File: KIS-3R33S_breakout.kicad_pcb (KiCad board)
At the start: 2 copper layers, 5 parts, among them P1 Screw terminal, P2 Screw terminal, U1 KIS-3R33S_modif

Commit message: Throwing parts around.
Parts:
- added C1: 1mF, 25V, Capacitors_SMD:c_elec_SMD_12.5x13.5, F.Cu at (172.0, 100.0)
- moved P2 16.6 mm to (184.7, 100.0)
- moved R1 13.0 mm to (182.3, 91.9)
- moved P1 10.8 mm to (130.6, 100.0)
- moved U1 9.20 mm to (150.0, 100.0)
- moved D1 7.07 mm to (186.8, 91.9)
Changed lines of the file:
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@@
 (kicad_pcb (version 4) (host pcbnew "(2015-05-01 BZR 5636)-product")
   (general
-    (links 8)
-    (no_connects 8)
-    (area 116.607142 92.155 182.14846 121.75)
+    (links 10)
+    (no_connects 10)
+    (area 124.607142 87.3 190.642858 112.6)
     (thickness 1.6)
     (drawings 0)
     (tracks 0)
     (zones 0)
-    (modules 5)
+    (modules 6)
     (nets 5)
   )
@@
   )
   (module DC-DC-modules:KIS-3R33S (layer F.Cu)
-    (at 149 109.15)
+    (at 150 100)
     (descr ./Docs/KIS-3R33S.pdf)
     (tags "DC-DC, buck, KIS-3R33S")
-    (fp_text reference U1 (at 0.05 11.6) (layer F.SilkS)
+    (fp_text reference U1 (at 0.05 11.6) (layer F.SilkS) hide
       (effects (font (size 1 1) (thickness 0.2)))
     )
@@
   )
   (module LEDs:LED-0805 (layer F.Cu)
-    (at 180.3 94.55)
+    (at 186.85 91.9)
     (descr "LED 0805 smd package")
     (tags "LED 0805 SMD")
     (attr smd)
-    (fp_text reference D1 (at 0 -1.27) (layer F.SilkS)
+    (fp_text reference D1 (at -0.1 1.8) (layer F.SilkS)
       (effects (font (size 1 1) (thickness 0.15)))
     )
@@
   )
   (module my_parts:MADW__SCREW_TERMINAL_2pin (layer F.Cu)
-    (at 122.55 107.2 180)
-    (fp_text reference P1 (at 0.01 -6.23 180) (layer F.SilkS)
-      (effects (font (size 1 1) (thickness 0.2)))
-    )
-    (fp_text value "Screw terminal" (at 0 6.71 180) (layer F.SilkS)
+    (at 130.55 100 180)
+    (fp_text reference P1 (at 0.01 -6.23 180) (layer F.SilkS) hide
+      (effects (font (size 1 1) (thickness 0.2)))
+    )
+    (fp_text value "Screw terminal" (at 0 6.71 180) (layer F.SilkS) hide
       (effects (font (size 1 1) (thickness 0.2)))
     )
@@
   )
   (module my_parts:MADW__SCREW_TERMINAL_2pin (layer F.Cu)
-    (at 170.7 108.9)
-    (fp_text reference P2 (at 0.01 -6.23) (layer F.SilkS)
-      (effects (font (size 1 1) (thickness 0.2)))
-    )
-    (fp_text value "Screw terminal" (at 0 6.71) (layer F.SilkS)
+    (at 184.7 100)
+    (fp_text reference P2 (at 0.01 -6.23) (layer F.SilkS) hide
+      (effects (font (size 1 1) (thickness 0.2)))
+    )
+    (fp_text value "Screw terminal" (at 0 6.71) (layer F.SilkS) hide
       (effects (font (size 1 1) (thickness 0.2)))
     )
@@
   )
   (module Resistors_SMD:R_0603_HandSoldering (layer F.Cu)
-    (at 179.2 104.55)
+    (at 182.3 91.9)
     (descr "Resistor SMD 0603, hand soldering")
     (tags "resistor 0603")
     (attr smd)
-    (fp_text reference R1 (at 0 -1.9) (layer F.SilkS)
+    (fp_text reference R1 (at 0.1 1.8) (layer F.SilkS)
       (effects (font (size 1 1) (thickness 0.15)))
     )
@@
     )
   )
+  (module Capacitors_SMD:c_elec_SMD_12.5x13.5 (layer F.Cu)
+    (at 172 100 90)
+    (descr "SMT capacitor, aluminium electrolytic, 12.5x13.5")
+    (fp_text reference C1 (at 8.6 -0.05 180) (layer F.SilkS) hide
+      (effects (font (size 1 1) (thickness 0.15)))
+    )
+    (fp_text value "1mF, 25V" (at 0 8 90) (layer F.Fab) hide
+      (effects (font (size 1 1) (thickness 0.15)))
+    )
+    (fp_line (start 3.95 -6.75) (end 6.75 -3.95) (layer F.SilkS) (width 0.15))
+    (fp_line (start 6.75 3.95) (end 3.95 6.75) (layer F.SilkS) (width 0.15))
+    (fp_line (start -6.15 1.1) (end -6.15 -1.1) (layer F.SilkS) (width 0.15))
+    (fp_line (start -6.1 1.35) (end -6.1 -1.35) (layer F.SilkS) (width 0.15))
+    (fp_line (start -6 -1.7) (end -6 1.7) (layer F.SilkS) (width 0.15))
+    (fp_line (start -5.9 2.05) (end -5.9 -2.05) (layer F.SilkS) (width 0.15))
+    (fp_line (start -5.8 -2.3) (end -5.8 2.3) (layer F.SilkS) (width 0.15))
+    (fp_line (start -5.7 2.55) (end -5.7 -2.55) (layer F.SilkS) (width 0.15))
+    (fp_line (start -5.6 2.75) (end -5.6 -2.75) (layer F.SilkS) (width 0.15))
+    (fp_line (start -5.5 -2.95) (end -5.5 2.95) (layer F.SilkS) (width 0.15))
+    (fp_line (start -5.4 3.1) (end -5.4 -3.1) (layer F.SilkS) (width 0.15))
+    (fp_line (start -5.3 -3.3) (end -5.3 3.3) (layer F.SilkS) (width 0.15))
+    (fp_line (start -5.2 -3.45) (end -5.2 3.45) (layer F.SilkS) (width 0.15))
+    (fp_line (start -5.1 -3.6) (end -5.1 3.6) (layer F.SilkS) (width 0.15))
+    (fp_line (start -2.2 -0.45) (end -6.9 -0.45) (layer Dwgs.User) (width 0.15))
+    (fp_line (start -2.2 0.45) (end -2.2 -0.45) (layer Dwgs.User) (width 0.15))
+    (fp_line (start -6.9 0.45) (end -2.2 0.45) (layer Dwgs.User) (width 0.15))
+    (fp_line (start -6.9 -0.45) (end -6.9 0.45) (layer Dwgs.User) (width 0.15))
+    (fp_line (start 2.2 0.45) (end 2.2 -0.45) (layer Dwgs.User) (width 0.15))
+    (fp_line (start 6.9 0.45) (end 2.2 0.45) (layer Dwgs.User) (width 0.15))
+    (fp_line (start 6.9 -0.45) (end 6.9 0.45) (layer Dwgs.User) (width 0.15))
+    (fp_line (start 2.2 -0.45) (end 6.9 -0.45) (layer Dwgs.User) (width 0.15))
+    (fp_line (start -6.75 6.75) (end -6.75 -6.75) (layer F.SilkS) (width 0.15))
+    (fp_line (start 3.95 6.75) (end -6.75 6.75) (layer F.SilkS) (width 0.15))
+    (fp_line (start 6.75 -3.95) (end 6.75 3.95) (layer F.SilkS) (width 0.15))
+    (fp_line (start -6.75 -6.75) (end 3.95 -6.75) (layer F.SilkS) (width 0.15))
+    (fp_circle (center 0 0) (end 6.25 0) (layer F.SilkS) (width 0.15))
+    (fp_line (start 4.95 0) (end 3.45 0) (layer F.SilkS) (width 0.15))
+    (fp_line (start 4.2 -0.75) (end 4.2 0.75) (layer F.SilkS) (width 0.15))
+    (pad 1 smd rect (at 4.55 0 90) (size 6 2.5) (layers F.Cu F.Paste F.Mask)
+      (net 1 /Vout))
+    (pad 2 smd rect (at -4.55 0 90) (size 6 2.5) (layers F.Cu F.Paste F.Mask)
+      (net 4 GND))
+  )
 )

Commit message: Done?
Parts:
- added G***: LED_smile_silkscreen_6mm, led-smile:LED_smile_silkscreen_6mm, B.Cu at (160.0, 100.0)
- added G***: OSHW-logo_silkscreen_6mm, oshw-logo:OSHW-logo_silkscreen_6mm, B.Cu at (140.0, 100.0)
- added RV1: 100k, Potentiometers:trimmer-pot_side-adjust_TSR-3006P_TH, F.Cu at (173.2, 92.0)
- moved D1 17.4 mm to (183.5, 109.0)
- moved R1 15.1 mm to (183.5, 107.0)
- moved C1 2.77 mm to (171.4, 102.7)
- moved P1 1.00 mm to (131.6, 100.0)
- moved P2 1.00 mm to (183.7, 100.0)
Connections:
- U1 pad 6: (no net) -> /ADJ
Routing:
- net GND: track 0.00 -> 80.5 mm, vias 0 -> 1
- net /Vout: track 0.00 -> 48.5 mm
- net /ADJ: track 0.00 -> 15.0 mm
- net /Vin: track 0.00 -> 10.3 mm
- net Net-(D1-Pad1): track 0.00 -> 2.02 mm
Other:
- board outline added: 61.5 x 22 mm
- net class Default: trace_width 0.25 -> 0.5; via_dia 0.6 -> 1.5; via_drill 0.4 -> 0.65
- net class power added: clearance 0.2, trace_width 4, via_dia 1.5, via_drill 0.65
- board text added: "+"
- board text added: "-"
- board text added: "...22V"
- board text added: "INPUT"
- board text added: "KIS-3R33S_breakout 2015 - blog.spitzenpfeil.org"

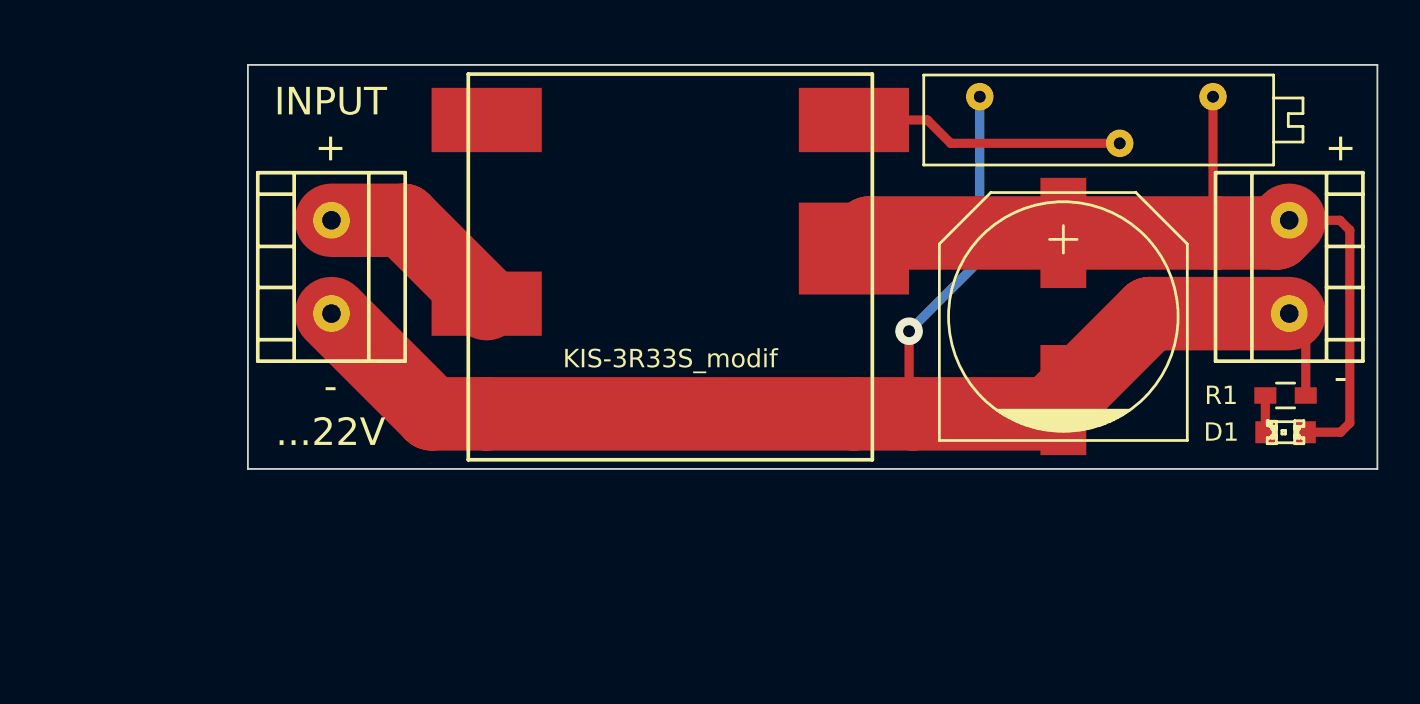
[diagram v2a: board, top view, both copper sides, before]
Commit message: Board-shrink.
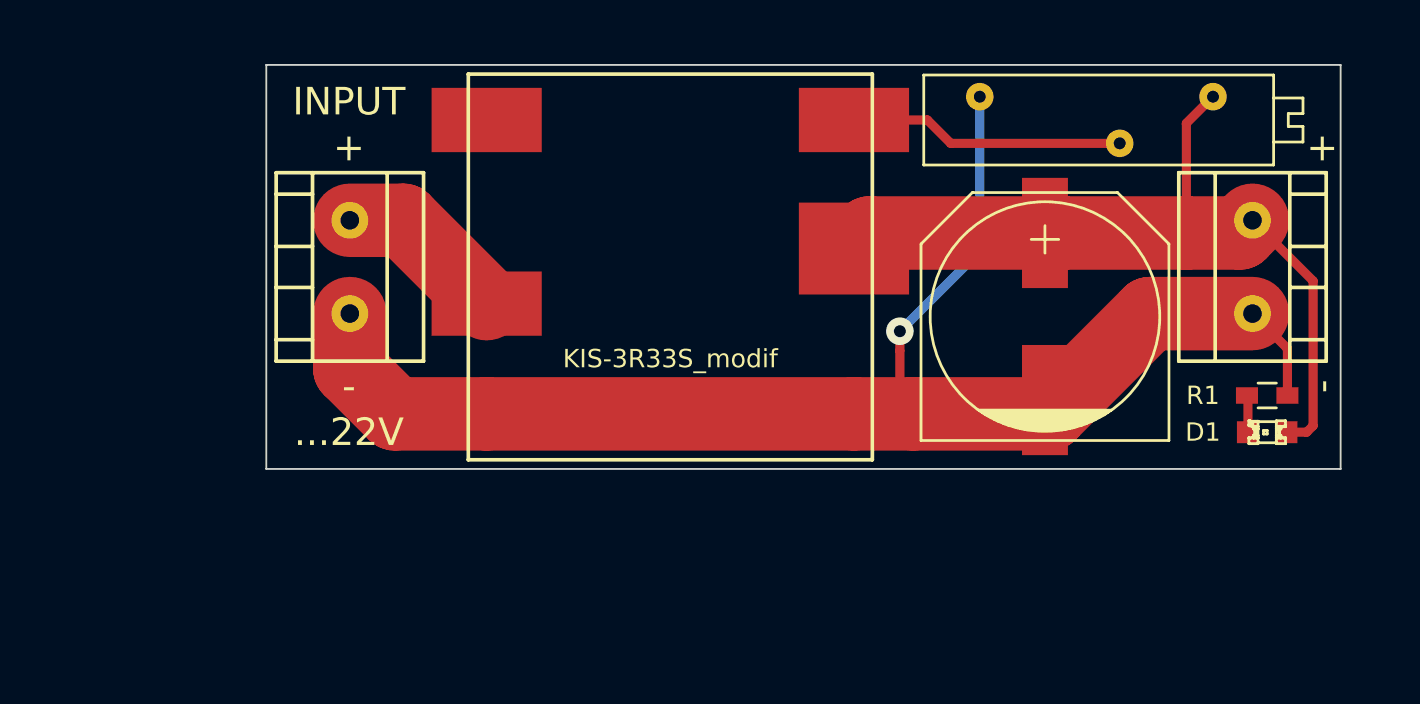
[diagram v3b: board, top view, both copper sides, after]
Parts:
- moved P2 2.00 mm to (181.7, 100.0)
- moved C1 1.00 mm to (170.4, 102.7)
- moved D1 1.00 mm to (182.5, 109.0)
- moved P1 1.00 mm to (132.6, 100.0)
- moved R1 1.00 mm to (182.5, 107.0)
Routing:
- net /Vout: track 48.5 -> 45.5 mm
- net /Vin: track 10.3 -> 9.33 mm
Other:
- board size 61.5 x 22 mm -> 58.5 x 22 mm

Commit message: Added optional descrete resistive-divider.
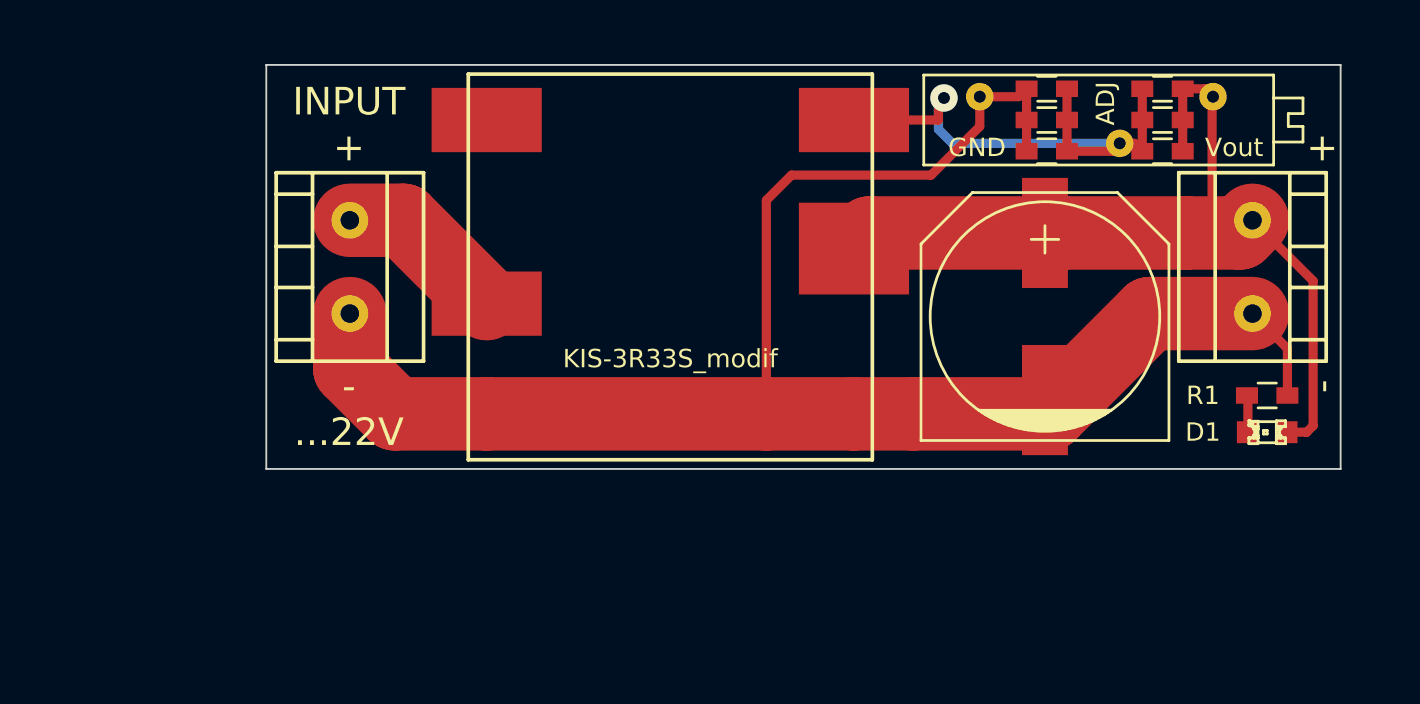
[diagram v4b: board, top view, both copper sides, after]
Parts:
- added R2: R, Resistors_SMD:R_0603_HandSoldering, F.Cu at (176.8, 90.3)
- added R3: R, Resistors_SMD:R_0603_HandSoldering, F.Cu at (170.5, 90.3)
- added R4: R, Resistors_SMD:R_0603_HandSoldering, F.Cu at (176.8, 92.0)
- added R5: R, Resistors_SMD:R_0603_HandSoldering, F.Cu at (170.5, 92.0)
- added R6: R, Resistors_SMD:R_0603_HandSoldering, F.Cu at (176.8, 93.7)
- added R7: R, Resistors_SMD:R_0603_HandSoldering, F.Cu at (170.5, 93.7)
- moved LOGO1 9.39 mm to (168.5, 104.0)
- moved LOGO2 9.39 mm to (148.5, 104.0)
- renumbered G*** to LOGO1, G*** to LOGO2
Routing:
- net GND: track 80.1 -> 94.4 mm, vias 1 -> 0
- net /ADJ: track 15.0 -> 29.3 mm, vias 0 -> 1
- net /Vout: track 45.5 -> 50.7 mm
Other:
- board text added: "ADJ"
- board text added: "GND"
- board text added: "KIS-3R33S_breakout V0.11.a 2015 - blog.spitzenpfeil.org"
- board text added: "Vout"
- board text removed: "KIS-3R33S_breakout 2015 - blog.spitzenpfeil.org"

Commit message: Adjustment pot was reversed. Vout should go up turning clockwise.
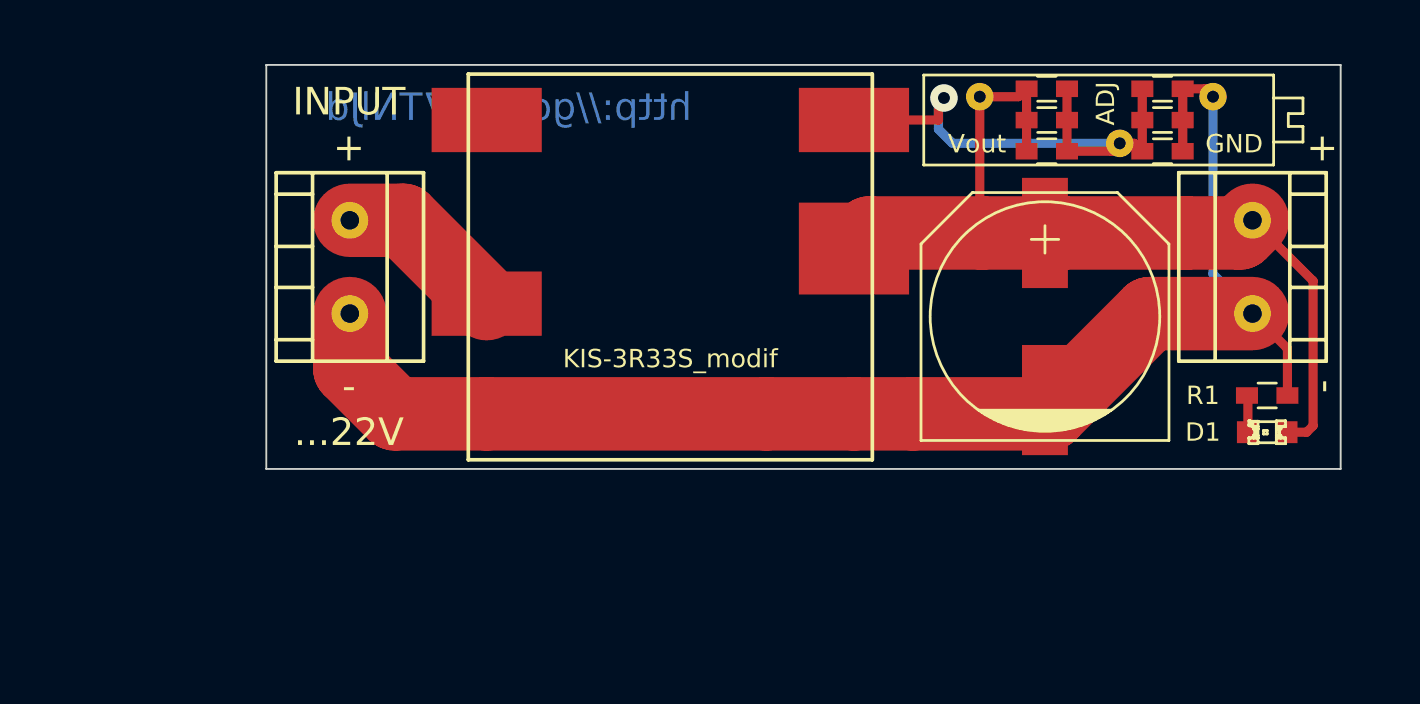
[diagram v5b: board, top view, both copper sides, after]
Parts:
- turned R2 to 0 degrees
- turned R3 to 0 degrees
- turned R4 to 0 degrees
- turned R5 to 0 degrees
- turned R6 to 0 degrees
- turned R7 to 0 degrees
- renumbered R3 to R2, R2 to R3, R5 to R4, R4 to R5, R7 to R6, R6 to R7
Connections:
- R2 pad 1: /ADJ -> /Vout
- R2 pad 2: GND -> /ADJ
- R3 pad 1: /Vout -> /ADJ
- R3 pad 2: /ADJ -> GND
- R4 pad 1: /ADJ -> /Vout
- R4 pad 2: GND -> /ADJ
- R5 pad 1: /Vout -> /ADJ
- R5 pad 2: /ADJ -> GND
- R6 pad 1: /ADJ -> /Vout
- R6 pad 2: GND -> /ADJ
- R7 pad 1: /Vout -> /ADJ
- R7 pad 2: /ADJ -> GND
- RV1 pad 1: GND -> /Vout
- RV1 pad 3: /Vout -> GND
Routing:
- net GND: track 94.4 -> 79.7 mm
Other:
- board text added: "KIS-3R33S_breakout V0.12.a 2015 - blog.spitzenpfeil.org"
- board text added: "http://goo.gl/7TNlJd"
- board text removed: "KIS-3R33S_breakout V0.11.a 2015 - blog.spitzenpfeil.org"

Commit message: Board shrink.
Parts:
- C1: footprint Capacitors_SMD:c_elec_SMD_12.5x13.5 -> Capacitors:c_elec_SMD_12.5x13.5
- moved R2 0.50 mm to (170.0, 90.3)
- moved R3 0.50 mm to (176.3, 90.3)
- moved R4 0.50 mm to (170.0, 92.0)
- moved R5 0.50 mm to (176.3, 92.0)
- moved R6 0.50 mm to (170.0, 93.7)
- moved R7 0.50 mm to (176.3, 93.7)
- moved RV1 0.50 mm to (172.7, 92.0)
- moved C1 0.25 mm to (170.2, 102.7)
- moved D1 0.25 mm to (182.2, 109.0)
- moved P2 0.25 mm to (181.4, 100.0)
- moved R1 0.25 mm to (182.2, 107.0)
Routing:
- net /Vout: track 51.1 -> 50.0 mm
- net GND: track 79.7 -> 80.6 mm
- net /ADJ: track 29.3 -> 28.5 mm
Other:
- board size 58.5 x 22 mm -> 57.4 x 21.6 mm
- board text added: "KIS-3R33S_breakout V0.12.b 2015 - blog.spitzenpfeil.org"
- board text removed: "KIS-3R33S_breakout V0.12.a 2015 - blog.spitzenpfeil.org"

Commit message: Silkscreen tweaks.
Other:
- board text added: "KIS-3R33S_breakout V0.12.c 2015 - blog.spitzenpfeil.org"
- board text removed: "KIS-3R33S_breakout V0.12.b 2015 - blog.spitzenpfeil.org"

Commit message: Added 'Snake' to silkscreen.
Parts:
- added G***: LOGO, LOGO, B.Cu at (157.5, 97.8)
- moved LOGO2 16.5 mm to (132.3, 107.0)
- moved LOGO1 13.9 mm to (182.1, 107.0)
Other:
- board text added: "KIS-3R33S_breakout V0.12.d 2015 - blog.spitzenpfeil.org"
- board text removed: "KIS-3R33S_breakout V0.12.c 2015 - blog.spitzenpfeil.org"
